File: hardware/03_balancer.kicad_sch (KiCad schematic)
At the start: 0 parts

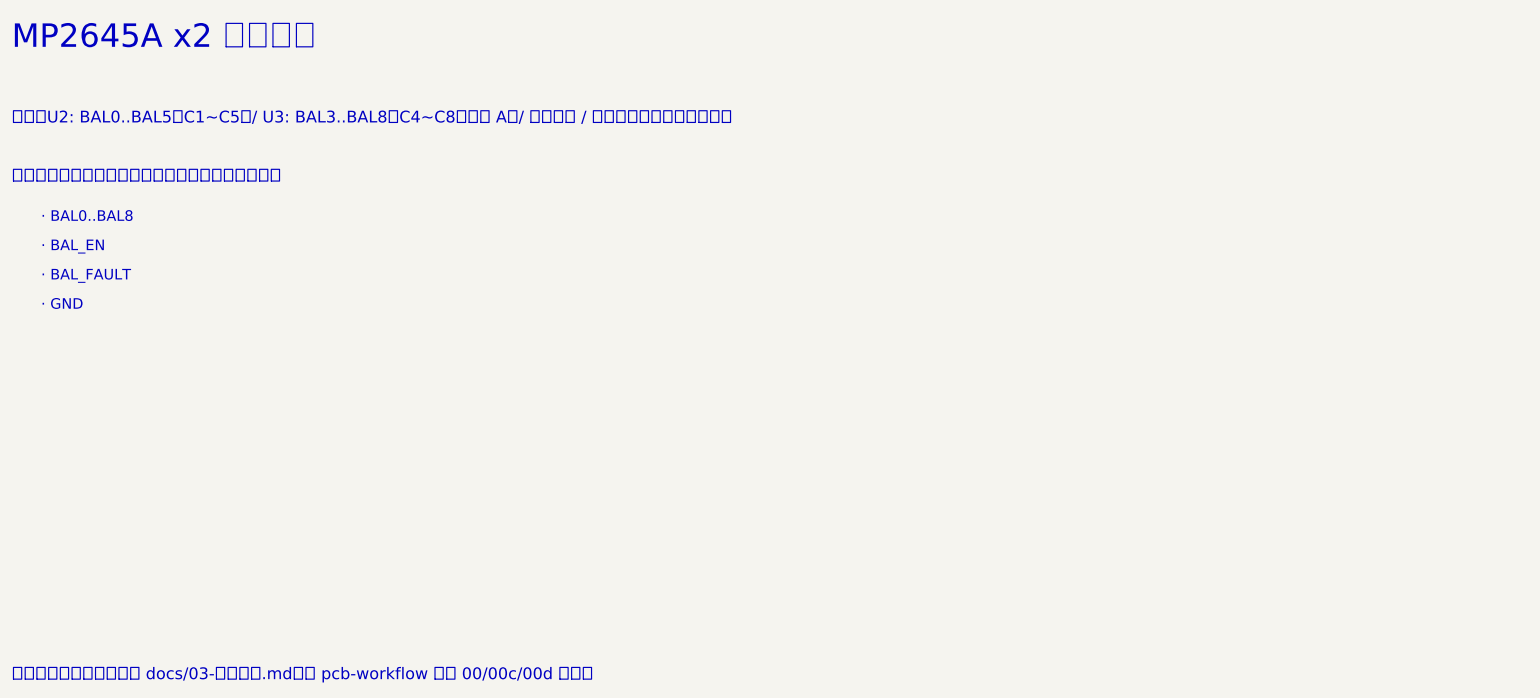
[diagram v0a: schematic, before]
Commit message: v0.3：主动均衡改为 MP2643 ×7（MPS 客供），光耦跨电位控制，逐对均衡策略，BOM 与成本估算
- docs/03：均衡章节按 MP2643 手册 Rev1.1 重写（外围逐件点名、电流/限压计算、光耦接口、线束与发热）
- firmware：7 对 EN/MODE 输出，边界电荷盈亏定方向，相邻不同时开，收敛仿真测试
- tools/bms_calc.py：MP2643 手册公式；tools/jlc_api.py：嘉立创料号接口；tools/cost.py：成本估算
- docs/02-BOM.csv v0.3（81 行，带立创编号与来源），docs/05-成本估算.md
- KiCad 骨架更新（03 子图接口、网络类）

Co-Authored-By: Claude Opus 5.5 <noreply@anthropic.com>
Claude-Session: https://claude.ai/code/session_01EyFjq1nqLUmfVYESj2uYXd
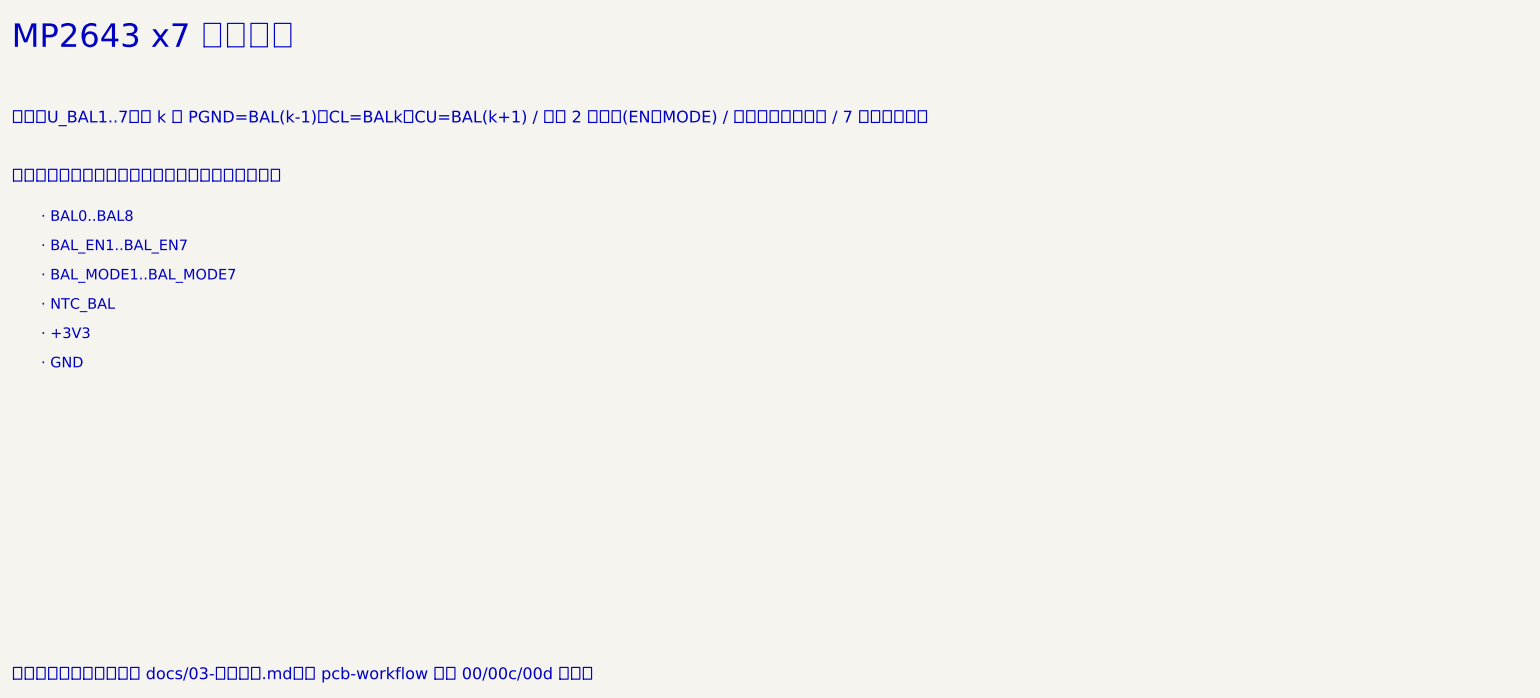
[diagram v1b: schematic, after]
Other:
- note added: "MP2643 x7 主动均衡"
- note added: "· +3V3"
- note added: "· BAL_EN1..BAL_EN7"
- note added: "· BAL_MODE1..BAL_MODE7"
- note added: "· NTC_BAL"
- note added: "内容：U_BAL1..7：第 k 颗 PGND=BAL(k-1)、CL=BALk、CU=BAL(k+1) / 每颗 2 只光耦(EN、MODE) / 电感下方全层禁铜 / 7 个本地地铜岛"
- note removed: "MP2645A x2 主动均衡"
- note removed: "· BAL_EN"
- note removed: "· BAL_FAULT"
- note removed: "内容：U2: BAL0..BAL5（C1~C5）/ U3: BAL3..BAL8（C4~C8，方案 A）/ 单线级联 / 功率电感（下方全层禁铜）"
- title: MP2645A x2 主动均衡 -> MP2643 x7 主动均衡
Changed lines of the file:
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@@
 	(paper "A3")
 	(title_block
-		(title "MP2645A x2 主动均衡")
+		(title "MP2643 x7 主动均衡")
 		(date "2026-09-26")
-		(rev "v0.2-skeleton")
+		(rev "v0.3-skeleton")
 		(company "MP2645A-BMS")
-		(comment 1 "8S LiFePO4 200A BMS · MPS MP2797 + MP2645A")
+		(comment 1 "8S LiFePO4 200A BMS · MPS MP2797 + MP2643x7")
 	)
-	(text "MP2645A x2 主动均衡"
+	(text "MP2643 x7 主动均衡"
 		(exclude_from_sim no)
 		(at 20 20 0)
@@
 		)
 	)
-	(text "内容：U2: BAL0..BAL5（C1~C5）/ U3: BAL3..BAL8（C4~C8，方案 A）/ 单线级联 / 功率电感（下方全层禁铜）"
+	(text "内容：U_BAL1..7：第 k 颗 PGND=BAL(k-1)、CL=BALk、CU=BAL(k+1) / 每颗 2 只光耦(EN、MODE) / 电感下方全层禁铜 / 7 个本地地铜岛"
 		(exclude_from_sim no)
 		(at 20 35 0)
@@
 		)
 	)
-	(text "· BAL_EN"
+	(text "· BAL_EN1..BAL_EN7"
 		(exclude_from_sim no)
 		(at 25 57 0)
@@
 		)
 	)
-	(text "· BAL_FAULT"
+	(text "· BAL_MODE1..BAL_MODE7"
 		(exclude_from_sim no)
 		(at 25 62 0)
@@
 		)
 	)
-	(text "· GND"
+	(text "· NTC_BAL"
 		(exclude_from_sim no)
 		(at 25 67 0)
 		(effects
 			(font
+				(size 1.8 1.8)
+			)
+			(justify left top)
+		)
+	)
+	(text "· +3V3"
+		(exclude_from_sim no)
+		(at 25 72 0)
+		(effects
+			(font
+				(size 1.8 1.8)
+			)
+			(justify left top)
+		)
+	)
+	(text "· GND"
+		(exclude_from_sim no)
+		(at 25 77 0)
+		(effects
+			(font

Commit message: 主动均衡改为分立开关电容（方案 B）：均衡部分约 ¥186→¥35/块
- 8 个互补半桥 AO3400A/AO3401A（基础库）+ 74LVC1G17 本节供电驱动，7 级飞电容 3×100µF，MCU BAL_CLK 50kHz 逐级电容耦合
- 固件：单一时钟使能；顶部/静置才开；压差>300mV 或任一节<3.0V 禁止；测试 37/37
- 计算器：sc_equalizer 模型（100mV≈0.21A，300mV≈0.62A）；测试 21/21
- BOM/成本：整板元器件 10 块 ¥359→¥202/块，100 块 ¥267→¥156/块
- 均衡端子改国产 2×5 Micro-Fit 兼容 C3030WV-2x5P（实测 3.0mm），节点保险丝 3A 1206

Co-Authored-By: Claude Opus 5.5 <noreply@anthropic.com>
Claude-Session: https://claude.ai/code/session_01EyFjq1nqLUmfVYESj2uYXd
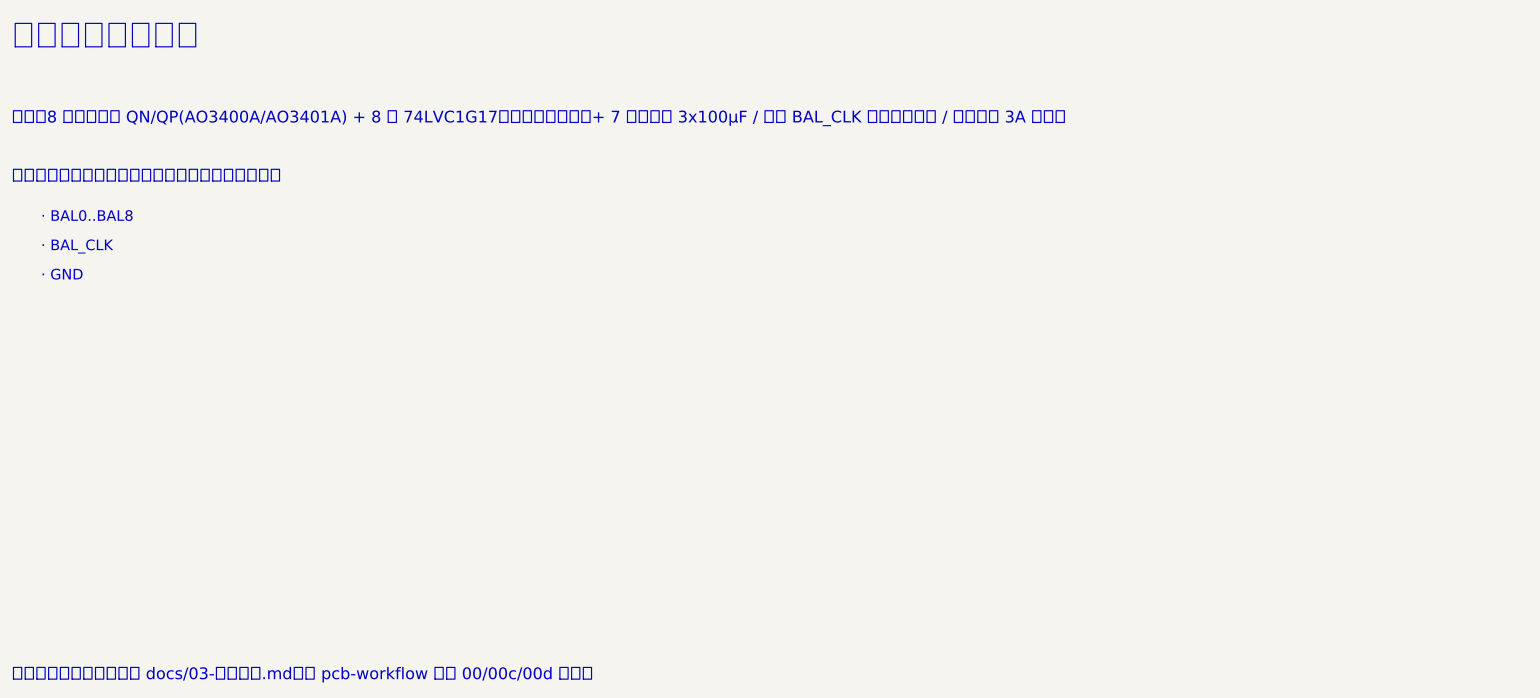
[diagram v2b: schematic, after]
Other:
- note added: "· BAL_CLK"
- note added: "内容：8 个互补半桥 QN/QP(AO3400A/AO3401A) + 8 个 74LVC1G17（本节电芯供电）+ 7 级飞电容 3x100µF / 时钟 BAL_CLK 逐级电容耦合 / 均衡节点 3A 保险丝"
- note added: "开关电容主动均衡"
- note removed: "MP2643 x7 主动均衡"
- note removed: "· +3V3"
- note removed: "· BAL_EN1..BAL_EN7"
- note removed: "· BAL_MODE1..BAL_MODE7"
- note removed: "· NTC_BAL"
- note removed: "内容：U_BAL1..7：第 k 颗 PGND=BAL(k-1)、CL=BALk、CU=BAL(k+1) / 每颗 2 只光耦(EN、MODE) / 电感下方全层禁铜 / 7 个本地地铜岛"
- title: MP2643 x7 主动均衡 -> 开关电容主动均衡
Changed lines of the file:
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@@
 	(paper "A3")
 	(title_block
-		(title "MP2643 x7 主动均衡")
+		(title "开关电容主动均衡")
 		(date "2026-09-26")
 		(rev "v0.3-skeleton")
 		(company "MP2645A-BMS")
-		(comment 1 "8S LiFePO4 200A BMS · MPS MP2797 + MP2643x7")
+		(comment 1 "8S LiFePO4 200A BMS · MPS MP2797 + 开关电容均衡")
 	)
-	(text "MP2643 x7 主动均衡"
+	(text "开关电容主动均衡"
 		(exclude_from_sim no)
 		(at 20 20 0)
@@
 		)
 	)
-	(text "内容：U_BAL1..7：第 k 颗 PGND=BAL(k-1)、CL=BALk、CU=BAL(k+1) / 每颗 2 只光耦(EN、MODE) / 电感下方全层禁铜 / 7 个本地地铜岛"
+	(text "内容：8 个互补半桥 QN/QP(AO3400A/AO3401A) + 8 个 74LVC1G17（本节电芯供电）+ 7 级飞电容 3x100µF / 时钟 BAL_CLK 逐级电容耦合 / 均衡节点 3A 保险丝"
 		(exclude_from_sim no)
 		(at 20 35 0)
@@
 		)
 	)
-	(text "· BAL_EN1..BAL_EN7"
+	(text "· BAL_CLK"
 		(exclude_from_sim no)
 		(at 25 57 0)
@@
 		)
 	)
-	(text "· BAL_MODE1..BAL_MODE7"
+	(text "· GND"
 		(exclude_from_sim no)
 		(at 25 62 0)
 		(effects
 			(font
-				(size 1.8 1.8)
-			)
-			(justify left top)
-		)
-	)
-	(text "· NTC_BAL"
-		(exclude_from_sim no)
-		(at 25 67 0)
-		(effects
-			(font
-				(size 1.8 1.8)
-			)
-			(justify left top)
-		)
-	)
-	(text "· +3V3"
-		(exclude_from_sim no)
-		(at 25 72 0)
-		(effects
-			(font
-				(size 1.8 1.8)
-			)
-			(justify left top)
-		)
-	)
-	(text "· GND"
-		(exclude_from_sim no)
-		(at 25 77 0)
-		(effects
-			(font
